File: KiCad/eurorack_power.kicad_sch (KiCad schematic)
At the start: 20 parts, among them J5 Eurorack Connector, U1 TL072, U2 TL072

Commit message: adding footprints
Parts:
- C10, C11, C12, C13, C14, C15, C16, C17, C8, C9, FB1, FB2, FB3, TP1, TP2, TP3, TP4, U2: now left out of the parts list
- J5: footprint (none) -> Connector_IDC:IDC-Header_2x08_P2.54mm_Vertical; now left out of the parts list
- U1: footprint (none) -> Package_SO:SOIC-8_3.9x4.9mm_P1.27mm; now left out of the parts list
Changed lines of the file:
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@@
 		(unit 1)
 		(exclude_from_sim no)
-		(in_bom yes)
+		(in_bom no)
 		(on_board yes)
 		(dnp no)
@@
 		)
 		(instances
-			(project ""
+			(project "Synced_LFO"
 				(path "/0124ec7f-ce8c-4d11-9a4b-6b8a0b3bcd3e/ae96ab4b-34eb-4fab-bc0d-5b970a07b467"
 					(reference "C8")
@@
 		)
 		(instances
-			(project ""
+			(project "Synced_LFO"
 				(path "/0124ec7f-ce8c-4d11-9a4b-6b8a0b3bcd3e/ae96ab4b-34eb-4fab-bc0d-5b970a07b467"
 					(reference "#PWR031")
@@
 		(unit 1)
 		(exclude_from_sim no)
-		(in_bom yes)
+		(in_bom no)
 		(on_board yes)
 		(dnp no)
@@
 		)
 		(instances
-			(project ""
+			(project "Synced_LFO"
 				(path "/0124ec7f-ce8c-4d11-9a4b-6b8a0b3bcd3e/ae96ab4b-34eb-4fab-bc0d-5b970a07b467"
 					(reference "C15")
@@
 		)
 		(instances
-			(project ""
+			(project "Synced_LFO"
 				(path "/0124ec7f-ce8c-4d11-9a4b-6b8a0b3bcd3e/ae96ab4b-34eb-4fab-bc0d-5b970a07b467"
 					(reference "#PWR032")
@@
 		)
 		(instances
-			(project ""
+			(project "Synced_LFO"
 				(path "/0124ec7f-ce8c-4d11-9a4b-6b8a0b3bcd3e/ae96ab4b-34eb-4fab-bc0d-5b970a07b467"
 					(reference "#PWR038")
@@
 		)
 		(instances
-			(project ""
+			(project "Synced_LFO"
 				(path "/0124ec7f-ce8c-4d11-9a4b-6b8a0b3bcd3e/ae96ab4b-34eb-4fab-bc0d-5b970a07b467"
 					(reference "#PWR036")
@@
 		(unit 1)
 		(exclude_from_sim no)
-		(in_bom yes)
+		(in_bom no)
 		(on_board yes)
 		(dnp no)
@@
 		)
 		(instances
-			(project ""
+			(project "Synced_LFO"
 				(path "/0124ec7f-ce8c-4d11-9a4b-6b8a0b3bcd3e/ae96ab4b-34eb-4fab-bc0d-5b970a07b467"
 					(reference "FB2")
@@
 		(unit 1)
 		(exclude_from_sim no)
-		(in_bom yes)
+		(in_bom no)
 		(on_board yes)
 		(dnp no)
@@
 		)
 		(instances
-			(project ""
+			(project "Synced_LFO"
 				(path "/0124ec7f-ce8c-4d11-9a4b-6b8a0b3bcd3e/ae96ab4b-34eb-4fab-bc0d-5b970a07b467"
 					(reference "TP1")
@@
 		(unit 1)
 		(exclude_from_sim no)
-		(in_bom yes)
+		(in_bom no)
 		(on_board yes)
 		(dnp no)
@@
 		)
 		(instances
-			(project ""
+			(project "Synced_LFO"
 				(path "/0124ec7f-ce8c-4d11-9a4b-6b8a0b3bcd3e/ae96ab4b-34eb-4fab-bc0d-5b970a07b467"
 					(reference "C14")
@@
 		(unit 1)
 		(exclude_from_sim no)
-		(in_bom yes)
+		(in_bom no)
 		(on_board yes)
 		(dnp no)
@@
 		)
 		(instances
-			(project ""
+			(project "Synced_LFO"
 				(path "/0124ec7f-ce8c-4d11-9a4b-6b8a0b3bcd3e/ae96ab4b-34eb-4fab-bc0d-5b970a07b467"
 					(reference "C12")
@@
 		(unit 1)
 		(exclude_from_sim no)
-		(in_bom yes)
+		(in_bom no)
 		(on_board yes)
 		(dnp no)
@@
 		)
 		(instances
-			(project ""
+			(project "Synced_LFO"
 				(path "/0124ec7f-ce8c-4d11-9a4b-6b8a0b3bcd3e/ae96ab4b-34eb-4fab-bc0d-5b970a07b467"
 					(reference "C10")
@@
 		(unit 3)
 		(exclude_from_sim no)
-		(in_bom yes)
+		(in_bom no)
 		(on_board yes)
 		(dnp no)
@@
 		)
 		(instances
-			(project ""
+			(project "Synced_LFO"
 				(path "/0124ec7f-ce8c-4d11-9a4b-6b8a0b3bcd3e/ae96ab4b-34eb-4fab-bc0d-5b970a07b467"
 					(reference "U2")
@@
 		)
 		(instances
-			(project ""
+			(project "Synced_LFO"
 				(path "/0124ec7f-ce8c-4d11-9a4b-6b8a0b3bcd3e/ae96ab4b-34eb-4fab-bc0d-5b970a07b467"
 					(reference "#PWR042")
@@
 		)
 		(instances
-			(project ""
+			(project "Synced_LFO"
 				(path "/0124ec7f-ce8c-4d11-9a4b-6b8a0b3bcd3e/ae96ab4b-34eb-4fab-bc0d-5b970a07b467"
 					(reference "#PWR041")
@@
 		)
 		(instances
-			(project ""
+			(project "Synced_LFO"
 				(path "/0124ec7f-ce8c-4d11-9a4b-6b8a0b3bcd3e/ae96ab4b-34eb-4fab-bc0d-5b970a07b467"
 					(reference "#PWR043")
@@
 		)
 		(instances
-			(project ""
+			(project "Synced_LFO"
 				(path "/0124ec7f-ce8c-4d11-9a4b-6b8a0b3bcd3e/ae96ab4b-34eb-4fab-bc0d-5b970a07b467"
 					(reference "#PWR035")
@@
 		(unit 1)
 		(exclude_from_sim no)
-		(in_bom yes)
+		(in_bom no)
 		(on_board yes)
 		(dnp no)
@@
 			)
 		)
-		(property "Footprint" ""
+		(property "Footprint" "Connector_IDC:IDC-Header_2x08_P2.54mm_Vertical"
 			(at 46.99 69.85 0)
 			(effects
@@
 		)
 		(instances
-			(project ""
+			(project "Synced_LFO"
 				(path "/0124ec7f-ce8c-4d11-9a4b-6b8a0b3bcd3e/ae96ab4b-34eb-4fab-bc0d-5b970a07b467"
 					(reference "J5")
@@
 		(unit 1)
 		(exclude_from_sim no)
-		(in_bom yes)
+		(in_bom no)
 		(on_board yes)
 		(dnp no)
@@
 		)
 		(instances
-			(project ""
+			(project "Synced_LFO"
 				(path "/0124ec7f-ce8c-4d11-9a4b-6b8a0b3bcd3e/ae96ab4b-34eb-4fab-bc0d-5b970a07b467"
 					(reference "C17")
@@
 		)
 		(instances
-			(project ""
+			(project "Synced_LFO"
 				(path "/0124ec7f-ce8c-4d11-9a4b-6b8a0b3bcd3e/ae96ab4b-34eb-4fab-bc0d-5b970a07b467"
 					(reference "#PWR030")
@@
 		(unit 3)
 		(exclude_from_sim no)
-		(in_bom yes)
+		(in_bom no)
 		(on_board yes)
 		(dnp no)
@@
 			)
 		)
-		(property "Footprint" ""
+		(property "Footprint" "Package_SO:SOIC-8_3.9x4.9mm_P1.27mm"
 			(at 57.15 142.24 0)
 			(effects
@@
 		)
 		(instances
-			(project ""
+			(project "Synced_LFO"
 				(path "/0124ec7f-ce8c-4d11-9a4b-6b8a0b3bcd3e/ae96ab4b-34eb-4fab-bc0d-5b970a07b467"
 					(reference "U1")
@@
 		)
 		(instances
-			(project ""
+			(project "Synced_LFO"
 				(path "/0124ec7f-ce8c-4d11-9a4b-6b8a0b3bcd3e/ae96ab4b-34eb-4fab-bc0d-5b970a07b467"
 					(reference "#FLG02")
@@
 		)
 		(instances
-			(project ""
+			(project "Synced_LFO"
 				(path "/0124ec7f-ce8c-4d11-9a4b-6b8a0b3bcd3e/ae96ab4b-34eb-4fab-bc0d-5b970a07b467"
 					(reference "#PWR040")
@@
 		)
 		(instances
-			(project ""
+			(project "Synced_LFO"
 				(path "/0124ec7f-ce8c-4d11-9a4b-6b8a0b3bcd3e/ae96ab4b-34eb-4fab-bc0d-5b970a07b467"
 					(reference "#PWR037")
@@
 		)
 		(instances
-			(project ""
+			(project "Synced_LFO"
 				(path "/0124ec7f-ce8c-4d11-9a4b-6b8a0b3bcd3e/ae96ab4b-34eb-4fab-bc0d-5b970a07b467"
 					(reference "#FLG01")
@@
 		(unit 1)
 		(exclude_from_sim no)
-		(in_bom yes)
+		(in_bom no)
 		(on_board yes)
 		(dnp no)
@@
 		)
 		(instances
-			(project ""
+			(project "Synced_LFO"
 				(path "/0124ec7f-ce8c-4d11-9a4b-6b8a0b3bcd3e/ae96ab4b-34eb-4fab-bc0d-5b970a07b467"
 					(reference "C16")
@@
 		)
 		(instances
-			(project ""
+			(project "Synced_LFO"
 				(path "/0124ec7f-ce8c-4d11-9a4b-6b8a0b3bcd3e/ae96ab4b-34eb-4fab-bc0d-5b970a07b467"
 					(reference "#PWR033")
@@
 		(unit 1)
 		(exclude_from_sim no)
-		(in_bom yes)
+		(in_bom no)
 		(on_board yes)
 		(dnp no)
@@
 		)
 		(instances
-			(project ""
+			(project "Synced_LFO"
 				(path "/0124ec7f-ce8c-4d11-9a4b-6b8a0b3bcd3e/ae96ab4b-34eb-4fab-bc0d-5b970a07b467"
 					(reference "FB1")
@@
 		(unit 1)
 		(exclude_from_sim no)
-		(in_bom yes)
+		(in_bom no)
 		(on_board yes)
 		(dnp no)
@@
 		)
 		(instances
-			(project ""
+			(project "Synced_LFO"
 				(path "/0124ec7f-ce8c-4d11-9a4b-6b8a0b3bcd3e/ae96ab4b-34eb-4fab-bc0d-5b970a07b467"
 					(reference "TP2")
@@
 		)
 		(instances
-			(project ""
+			(project "Synced_LFO"
 				(path "/0124ec7f-ce8c-4d11-9a4b-6b8a0b3bcd3e/ae96ab4b-34eb-4fab-bc0d-5b970a07b467"
 					(reference "#PWR034")
@@
 		(unit 1)
 		(exclude_from_sim no)
-		(in_bom yes)
+		(in_bom no)
 		(on_board yes)
 		(dnp no)
@@
 		)
 		(instances
-			(project ""
+			(project "Synced_LFO"
 				(path "/0124ec7f-ce8c-4d11-9a4b-6b8a0b3bcd3e/ae96ab4b-34eb-4fab-bc0d-5b970a07b467"
 					(reference "TP3")
@@
 		(unit 1)
 		(exclude_from_sim no)
-		(in_bom yes)
+		(in_bom no)
 		(on_board yes)
 		(dnp no)
@@
 		)
 		(instances
-			(project ""
+			(project "Synced_LFO"
 				(path "/0124ec7f-ce8c-4d11-9a4b-6b8a0b3bcd3e/ae96ab4b-34eb-4fab-bc0d-5b970a07b467"
 					(reference "C13")
@@
 		(unit 1)
 		(exclude_from_sim no)
-		(in_bom yes)
+		(in_bom no)
 		(on_board yes)
 		(dnp no)
@@
 		)
 		(instances
-			(project ""
+			(project "Synced_LFO"
 				(path "/0124ec7f-ce8c-4d11-9a4b-6b8a0b3bcd3e/ae96ab4b-34eb-4fab-bc0d-5b970a07b467"
 					(reference "TP4")
@@
 		(unit 1)
 		(exclude_from_sim no)
-		(in_bom yes)
+		(in_bom no)
 		(on_board yes)
 		(dnp no)
@@
 		)
 		(instances
-			(project ""
+			(project "Synced_LFO"
 				(path "/0124ec7f-ce8c-4d11-9a4b-6b8a0b3bcd3e/ae96ab4b-34eb-4fab-bc0d-5b970a07b467"
 					(reference "FB3")
@@
 		)
 		(instances
-			(project ""
+			(project "Synced_LFO"
 				(path "/0124ec7f-ce8c-4d11-9a4b-6b8a0b3bcd3e/ae96ab4b-34eb-4fab-bc0d-5b970a07b467"
 					(reference "#FLG03")
@@
 		(unit 1)
 		(exclude_from_sim no)
-		(in_bom yes)
+		(in_bom no)
 		(on_board yes)
 		(dnp no)
@@
 		)
 		(instances
-			(project ""
+			(project "Synced_LFO"
 				(path "/0124ec7f-ce8c-4d11-9a4b-6b8a0b3bcd3e/ae96ab4b-34eb-4fab-bc0d-5b970a07b467"
 					(reference "C11")
@@
 		(unit 1)
 		(exclude_from_sim no)
-		(in_bom yes)
+		(in_bom no)
 		(on_board yes)
 		(dnp no)
@@
 		)
 		(instances
-			(project ""
+			(project "Synced_LFO"
 				(path "/0124ec7f-ce8c-4d11-9a4b-6b8a0b3bcd3e/ae96ab4b-34eb-4fab-bc0d-5b970a07b467"
 					(reference "C9")

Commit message: adding last missing footprints
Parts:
- removed U1: TL072, Package_SO:SOIC-8_3.9x4.9mm_P1.27mm, symbol Amplifier_Operational:TL072
- removed U2: TL072, symbol Amplifier_Operational:TL072
- added U3, U4: TL072, Package_SO:SOIC-8_3.9x4.9mm_P1.27mm, symbol Amplifier_Operational:TL072
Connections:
- net +12V: now also U3.8 (V+), U4.8 (V+)
- net -12V: now also U3.4 (V-), U4.4 (V-)
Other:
- note added: "EURORACK POWER"
- note added: "TL072 OPAMP POWER AND FILTERING"
- moved on the sheet: C10, C11, C8, C9

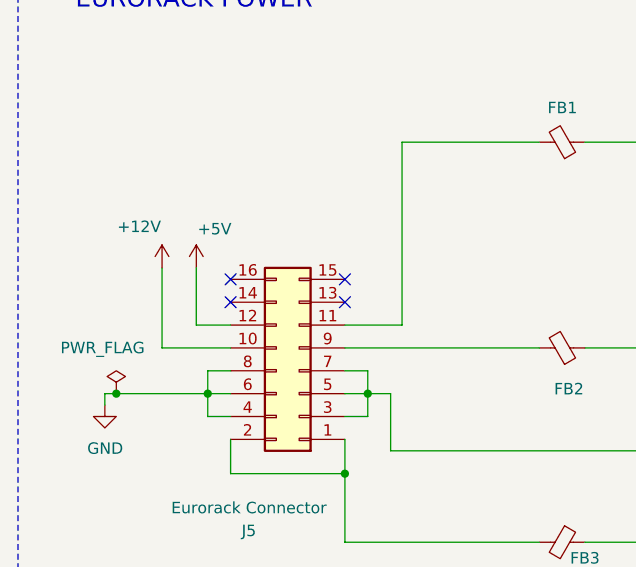
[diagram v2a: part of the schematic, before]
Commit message: fixing power in sch; placing components; connecting pads and coppering
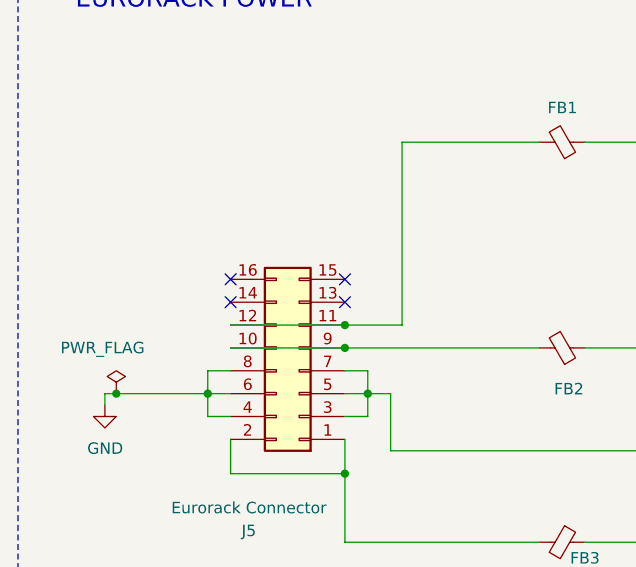
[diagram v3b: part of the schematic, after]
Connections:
- net +12V: no longer J5.10 (Pin_10)
- net +5V: no longer J5.12 (Pin_12)
- net at FB2.2, J5.9 (Pin_9): now also J5.10 (Pin_10)
- net at FB1.2, J5.11 (Pin_11): now also J5.12 (Pin_12)
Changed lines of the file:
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@@
+	)
+	(junction
+		(at 52.07 67.31)
+		(diameter 0)
+		(color 0 0 0 0)
+	)
+	(junction
+		(at 52.07 64.77)
+		(diameter 0)
+		(color 0 0 0 0)
 	)
 	(junction
@@
 	(wire
 		(pts
-			(xy 31.75 67.31) (xy 39.37 67.31)
-		)
-		(stroke
-			(width 0)
-			(type default)
-		)
-	)
-	(wire
-		(pts
 			(xy 52.07 69.85) (xy 54.61 69.85)
 		)
@@
 	(wire
 		(pts
+			(xy 39.37 67.31) (xy 52.07 67.31)
+		)
+		(stroke
+			(width 0)
+			(type default)
+		)
+	)
+	(wire
+		(pts
 			(xy 121.92 67.31) (xy 129.54 67.31)
 		)
@@
 	(wire
 		(pts
-			(xy 35.56 58.42) (xy 35.56 64.77)
-		)
-		(stroke
-			(width 0)
-			(type default)
-		)
-	)
-	(wire
-		(pts
 			(xy 58.42 44.45) (xy 73.66 44.45)
 		)
@@
 	(wire
 		(pts
-			(xy 35.56 64.77) (xy 39.37 64.77)
-		)
-		(stroke
-			(width 0)
-			(type default)
-		)
-	)
-	(wire
-		(pts
 			(xy 36.83 74.93) (xy 39.37 74.93)
 		)
@@
 	(wire
 		(pts
-			(xy 31.75 58.42) (xy 31.75 67.31)
+			(xy 39.37 64.77) (xy 52.07 64.77)
 		)
 		(stroke
@@
 	)
 	(symbol
-		(lib_name "+12V_1")
-		(lib_id "power:+12V")
-		(at 31.75 58.42 0)
-		(mirror y)
-		(unit 1)
-		(exclude_from_sim no)
-		(in_bom yes)
-		(on_board yes)
-		(dnp no)
-		(fields_autoplaced yes)
-		(property "Reference" "#PWR033"
-			(at 31.75 62.23 0)
-			(effects
-				(font
-					(size 1.27 1.27)
-				)
-				(hide yes)
-			)
-		)
-		(property "Value" "+12V"
-			(at 29.21 53.848 0)
-			(effects
-				(font
-					(size 1.27 1.27)
-				)
-			)
-		)
-		(property "Footprint" ""
-			(at 31.75 58.42 0)
-			(effects
-				(font
-					(size 1.27 1.27)
-				)
-				(hide yes)
-			)
-		)
-		(property "Datasheet" ""
-			(at 31.75 58.42 0)
-			(effects
-				(font
-					(size 1.27 1.27)
-				)
-				(hide yes)
-			)
-		)
-		(property "Description" "Power symbol creates a global label with name \"+12V\""
-			(at 31.75 58.42 0)
-			(effects
-				(font
-					(size 1.27 1.27)
-				)
-				(hide yes)
-			)
-		)
-		(pin "1"
-		)
-		(instances
-			(project "Synced_LFO"
-				(path "/0124ec7f-ce8c-4d11-9a4b-6b8a0b3bcd3e/ae96ab4b-34eb-4fab-bc0d-5b970a07b467"
-					(reference "#PWR033")
-					(unit 1)
-				)
-			)
-			(project "5 Sep Sequencer"
-				(path "/96e48c46-040c-48e5-b6d4-8ee98b2fce0b/4fa43ce6-75e2-4254-9dee-ae44702d62b6"
-					(reference "#PWR08")
-					(unit 1)
-				)
-			)
-		)
-	)
-	(symbol
 		(lib_id "Device:FerriteBead_Small")
 		(at 76.2 44.45 270)
@@
 					(unit 1)
 				)
-			)
-		)
-	)
-	(symbol
-		(lib_id "power:+5V")
-		(at 35.56 58.42 0)
-		(unit 1)
-		(exclude_from_sim no)
-		(in_bom yes)
-		(on_board yes)
-		(dnp no)
-		(fields_autoplaced yes)
-		(property "Reference" "#PWR034"
-			(at 35.56 62.23 0)
-			(effects
-				(font
-					(size 1.27 1.27)
-				)
-				(hide yes)
-			)
-		)
-		(property "Value" "+5V"
-			(at 37.592 54.102 0)
-			(effects
-				(font
-					(size 1.27 1.27)
-				)
-			)
-		)
-		(property "Footprint" ""
-			(at 35.56 58.42 0)
-			(effects
-				(font
-					(size 1.27 1.27)
-				)
-				(hide yes)
-			)
-		)
-		(property "Datasheet" ""
-			(at 35.56 58.42 0)
-			(effects
-				(font
-					(size 1.27 1.27)
-				)
-				(hide yes)
-			)
-		)
-		(property "Description" "Power symbol creates a global label with name \"+5V\""
-			(at 35.56 58.42 0)
-			(effects
-				(font
-					(size 1.27 1.27)
-				)
-				(hide yes)
-			)
-		)
-		(pin "1"
-		)
-		(instances
-			(project "Synced_LFO"
-				(path "/0124ec7f-ce8c-4d11-9a4b-6b8a0b3bcd3e/ae96ab4b-34eb-4fab-bc0d-5b970a07b467"
-					(reference "#PWR034")
-					(unit 1)
-				)
-			)
-			(project "5 Sep Sequencer"
-				(path "/96e48c46-040c-48e5-b6d4-8ee98b2fce0b/4fa43ce6-75e2-4254-9dee-ae44702d62b6"
-					(reference "#PWR06")
-					(unit 1)
-				)

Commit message: adding new logo
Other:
- company: (none) -> © Dirty Dream – Nathanael Noir
- title: (none) -> Chronophase LFO
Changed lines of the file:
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@@
 	(generator_version "9.0")
 	(paper "A4")
+	(title_block
+		(title "Chronophase LFO")
+		(date "2026-04-01")
+		(rev "v1.0")
+		(company "© Dirty Dream – Nathanael Noir")
+	)
 	(rectangle
 		(start 15.748 101.854)
